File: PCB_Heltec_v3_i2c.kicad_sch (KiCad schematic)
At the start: 9 parts, among them J1 i2c, J2 i2c, J3 i2c, J4 SPI, J5 Conn_01x04_Pin, J6 PINHD_1x4_Female, J7 PINHD_1x4_Female, U1 ESP32_LORA_V2.0

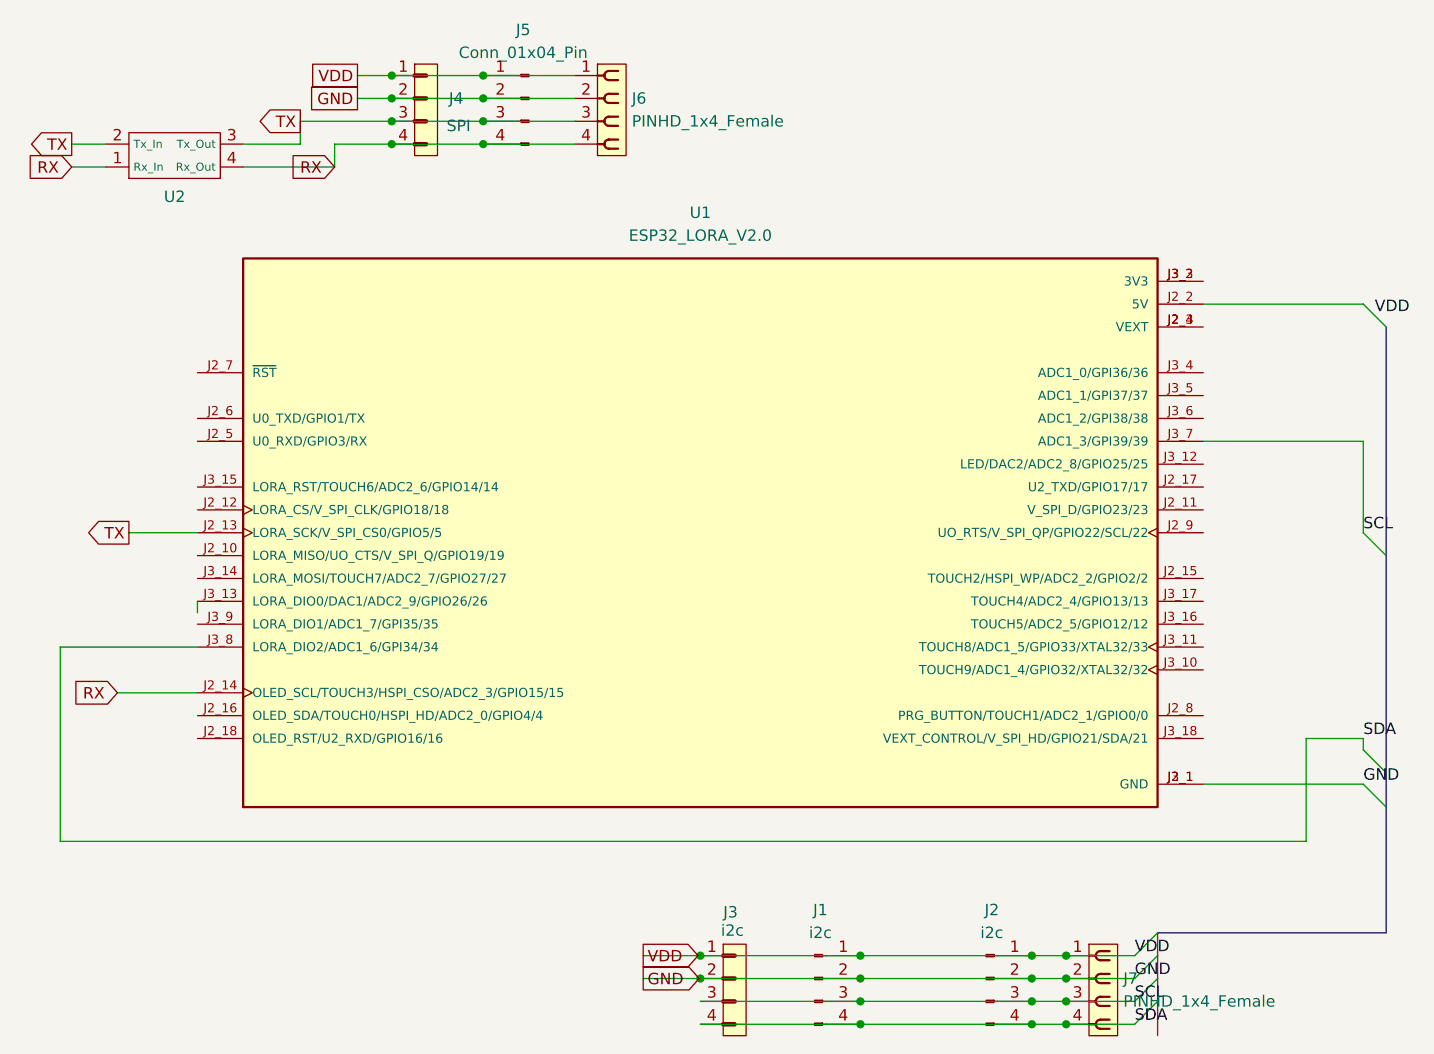
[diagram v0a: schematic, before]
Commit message: fix CDD net routing, replace rx/tx mux with pin header instead smd pads, reduce board width
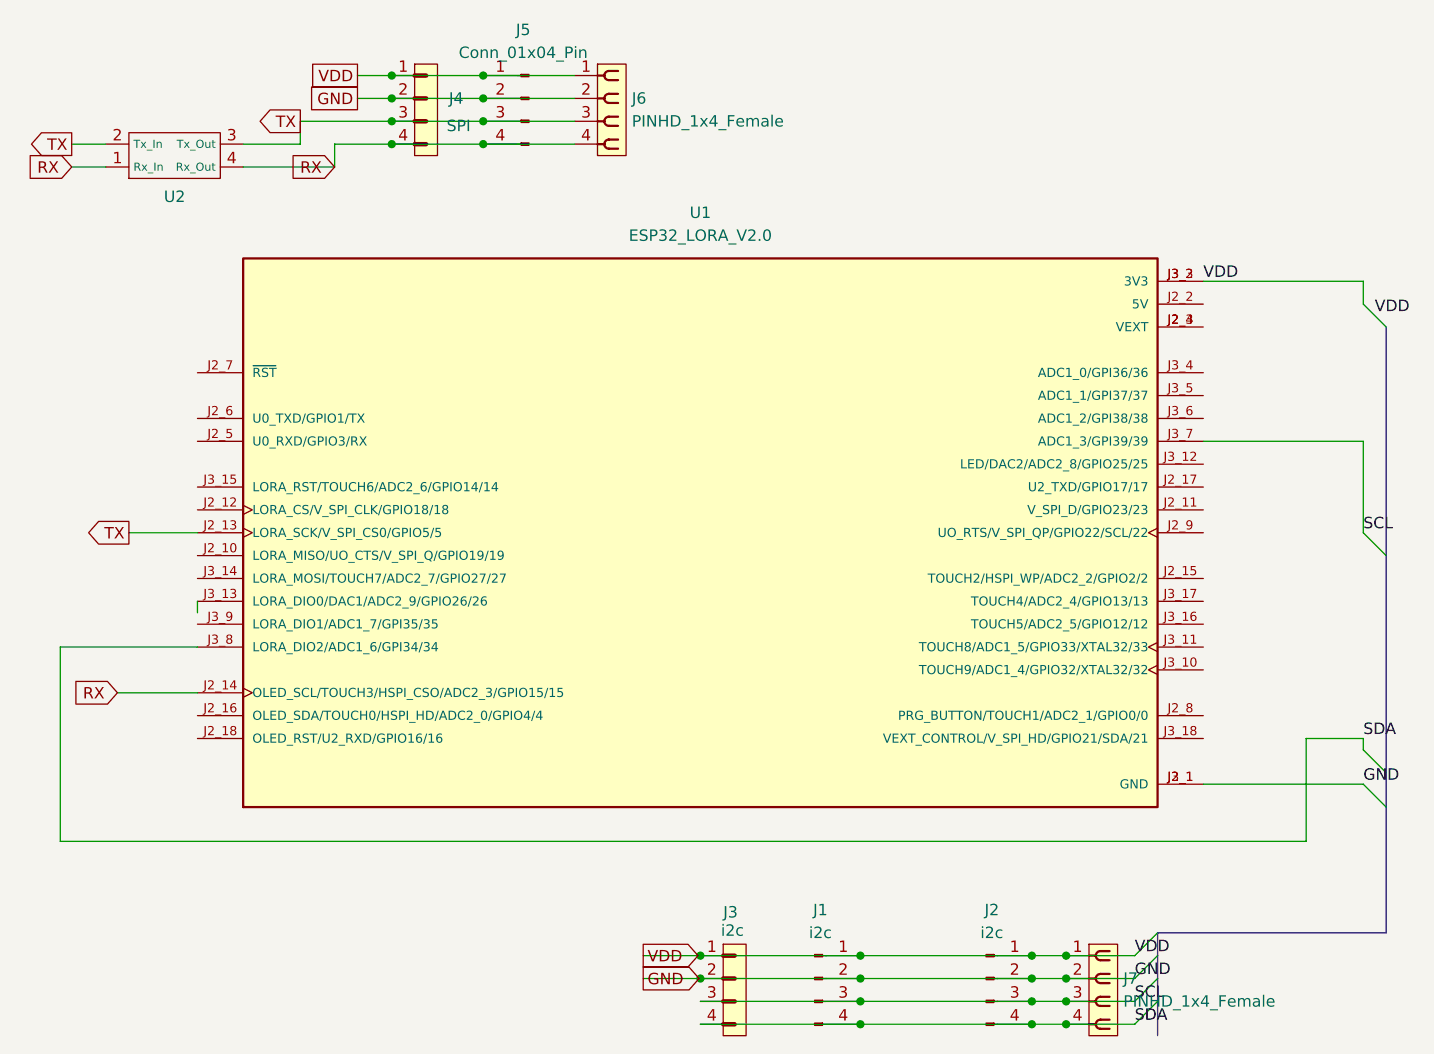
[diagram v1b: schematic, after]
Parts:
- U2: footprint PCB_Heltec_v3_i2c:poka-yoke_rxtx -> Connector_PinHeader_2.54mm:PinHeader_2x02_P2.54mm_Vertical
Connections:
- net VDD: now also U1.J3_2 (3V3), U1.J3_3 (3V3)
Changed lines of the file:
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@@
 (kicad_sch
-	(version 20231120)
+	(version 20250114)
 	(generator "eeschema")
-	(generator_version "8.0")
+	(generator_version "9.0")
 	(paper "A4")
 	(junction
@@
 	(wire
 		(pts
+			(xy 166.37 49.53) (xy 166.37 46.99)
+		)
+		(stroke
+			(width 0)
+			(type default)
+		)
+	)
+	(wire
+		(pts
 			(xy 110.49 121.92) (xy 129.54 121.92)
 		)
@@
 	(wire
 		(pts
-			(xy 148.59 49.53) (xy 166.37 49.53)
-		)
-		(stroke
-			(width 0)
-			(type default)
-		)
-	)
-	(wire
-		(pts
 			(xy 58.42 29.21) (xy 68.58 29.21)
 		)
@@
 		(pts
 			(xy 58.42 24.13) (xy 54.61 24.13)
+		)
+		(stroke
+			(width 0)
+			(type default)
+		)
+	)
+	(wire
+		(pts
+			(xy 148.59 46.99) (xy 166.37 46.99)
 		)
 		(stroke
@@
 	(label "SCL"
 		(at 166.37 74.93 0)
+		(effects
+			(font
+				(size 1.27 1.27)
+			)
+			(justify left bottom)
+		)
+	)
+	(label "VDD"
+		(at 148.59 46.99 0)
 		(effects
 			(font
@@
 			)
 		)
-		(property "Footprint" "PCB_Heltec_v3_i2c:poka-yoke_rxtx"
+		(property "Footprint" "Connector_PinHeader_2.54mm:PinHeader_2x02_P2.54mm_Vertical"
 			(at 35.56 29.21 0)
 			(effects
@@
 		)
 	)
+	(embedded_fonts no)
 )
